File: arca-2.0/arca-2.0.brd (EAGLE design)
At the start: 355.6 x 127 mm, 192 parts, among them IC1 MCP6N11R, IC2 MCP6N11R, IC3 MCP6N11R, IC4 MCP6N11R, IC5 LM324D, IC6 LM324D, SW1 1101M2S3CQE2, SW2 1101M2S3CQE2, T1 FQP30N06L, T2 FQP30N06L, T3 FQP30N06L, T4 FQP30N06L, T5 FQP30N06L, T6 FQP30N06L, X1 2540-5

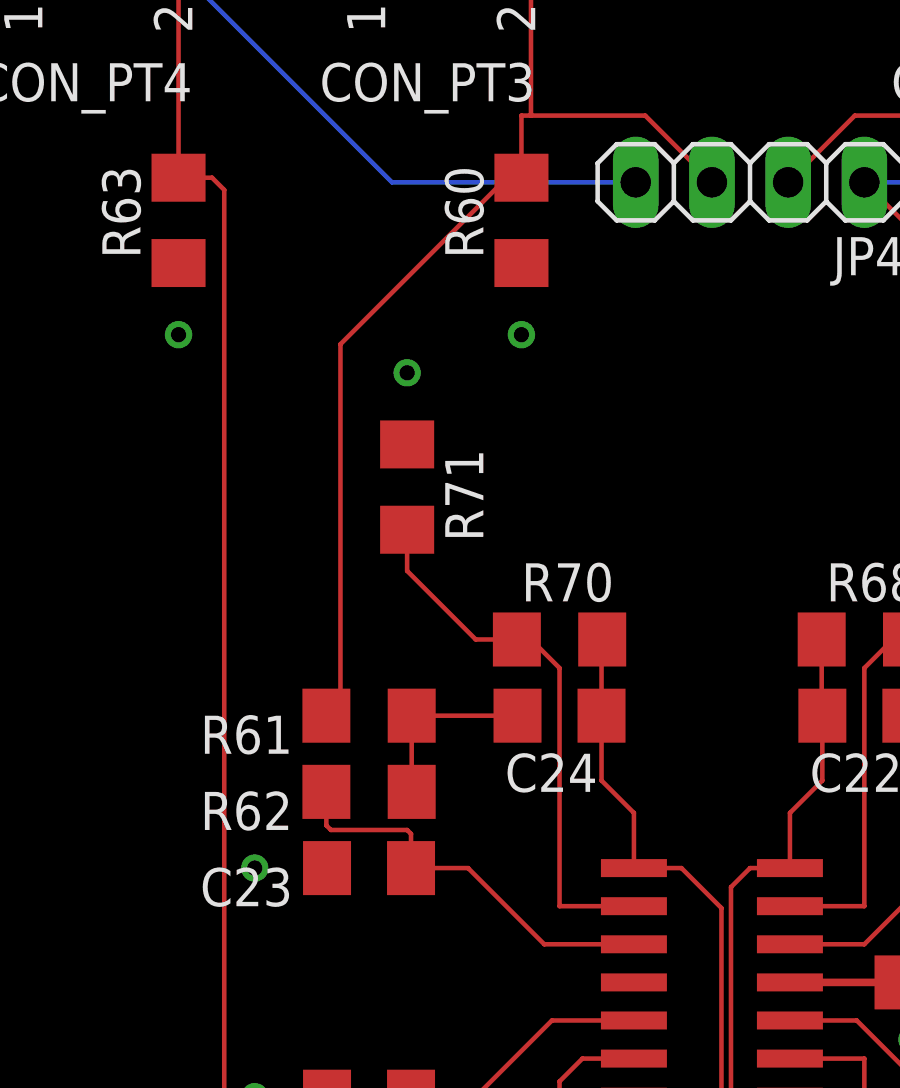
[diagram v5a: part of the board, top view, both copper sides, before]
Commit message: resistor cleanup for v_ref
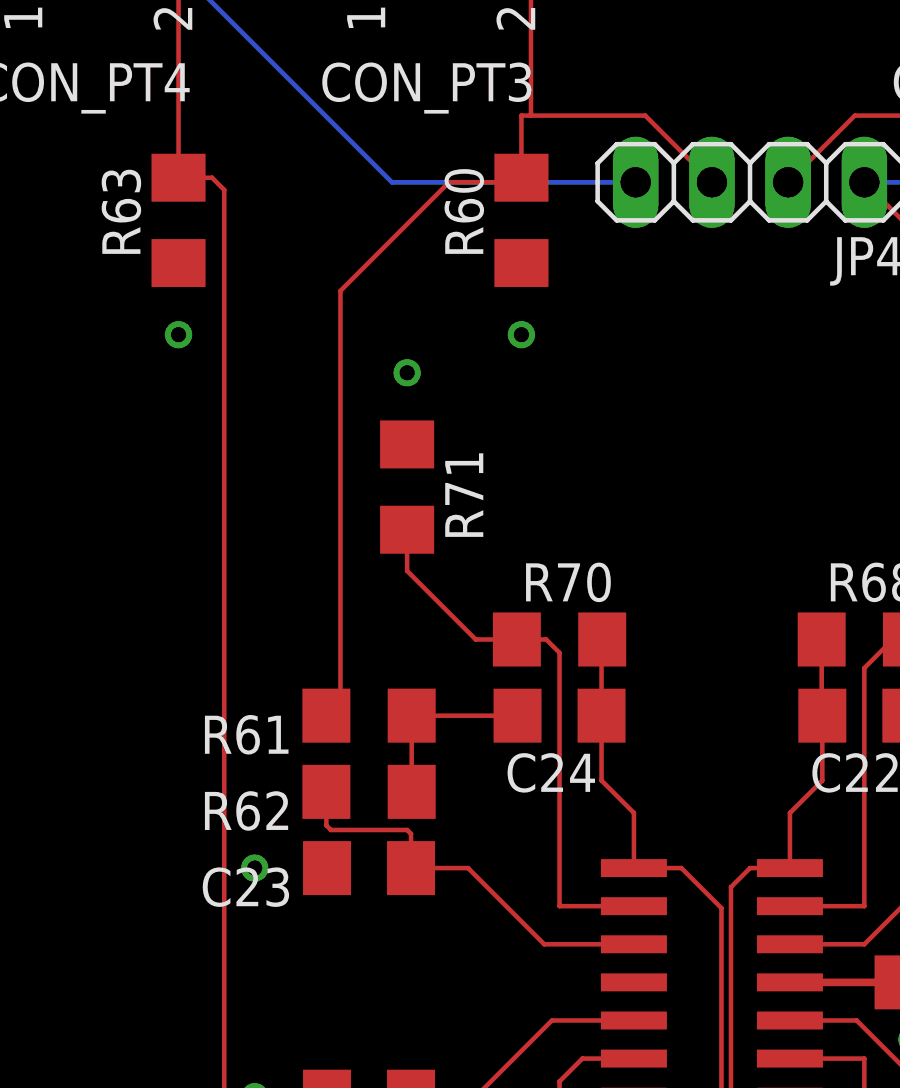
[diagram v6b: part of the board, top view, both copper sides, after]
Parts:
- R46, R48, R50, R52: value 10k -> 43k
- R47, R49, R51, R53: value 10k -> 11k
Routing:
- net PT3-: track 46.7 -> 47.7 mm
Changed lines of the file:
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@@
 <?xml version="1.0" encoding="utf-8"?>
 <!DOCTYPE eagle SYSTEM "eagle.dtd">
-<eagle version="9.5.0">
+<eagle version="9.6.2">
 <drawing>
 <settings>
@@
 <attribute name="VALUE" x="311.15" y="12.7" size="1.27" layer="27" rot="R270"/>
 </element>
-<element name="R46" library="rcl" library_urn="urn:adsk.eagle:library:334" package="R1206" package3d_urn="urn:adsk.eagle:package:23540/2" value="10k" x="139.7" y="81.28" smashed="yes">
+<element name="R46" library="rcl" library_urn="urn:adsk.eagle:library:334" package="R1206" package3d_urn="urn:adsk.eagle:package:23540/2" value="43k" x="139.7" y="81.28" smashed="yes">
 <attribute name="NAME" x="138.43" y="82.55" size="1.27" layer="25"/>
 <attribute name="POPULARITY" value="19" x="139.7" y="81.28" size="1.778" layer="27" display="off"/>
@@
 <attribute name="VALUE" x="138.43" y="78.74" size="1.27" layer="27"/>
 </element>
-<element name="R47" library="rcl" library_urn="urn:adsk.eagle:library:334" package="R1206" package3d_urn="urn:adsk.eagle:package:23540/2" value="10k" x="139.7" y="78.74" smashed="yes" rot="R180">
+<element name="R47" library="rcl" library_urn="urn:adsk.eagle:library:334" package="R1206" package3d_urn="urn:adsk.eagle:package:23540/2" value="11k" x="139.7" y="78.74" smashed="yes" rot="R180">
 <attribute name="NAME" x="140.97" y="77.47" size="1.27" layer="25" rot="R180"/>
 <attribute name="POPULARITY" value="19" x="139.7" y="78.74" size="1.778" layer="27" rot="R180" display="off"/>
@@
 <attribute name="VALUE" x="140.97" y="81.28" size="1.27" layer="27" rot="R180"/>
 </element>
-<element name="R48" library="rcl" library_urn="urn:adsk.eagle:library:334" package="R1206" package3d_urn="urn:adsk.eagle:package:23540/2" value="10k" x="118.11" y="81.28" smashed="yes">
+<element name="R48" library="rcl" library_urn="urn:adsk.eagle:library:334" package="R1206" package3d_urn="urn:adsk.eagle:package:23540/2" value="43k" x="118.11" y="81.28" smashed="yes">
 <attribute name="NAME" x="116.84" y="82.55" size="1.27" layer="25"/>
 <attribute name="POPULARITY" value="19" x="118.11" y="81.28" size="1.778" layer="27" display="off"/>
@@
 <attribute name="VALUE" x="116.84" y="78.74" size="1.27" layer="27"/>
 </element>
-<element name="R49" library="rcl" library_urn="urn:adsk.eagle:library:334" package="R1206" package3d_urn="urn:adsk.eagle:package:23540/2" value="10k" x="118.11" y="78.74" smashed="yes" rot="R180">
+<element name="R49" library="rcl" library_urn="urn:adsk.eagle:library:334" package="R1206" package3d_urn="urn:adsk.eagle:package:23540/2" value="11k" x="118.11" y="78.74" smashed="yes" rot="R180">
 <attribute name="NAME" x="119.38" y="77.47" size="1.27" layer="25" rot="R180"/>
 <attribute name="POPULARITY" value="19" x="118.11" y="78.74" size="1.778" layer="27" rot="R180" display="off"/>
@@
 <attribute name="VALUE" x="119.38" y="81.28" size="1.27" layer="27" rot="R180"/>
 </element>
-<element name="R50" library="rcl" library_urn="urn:adsk.eagle:library:334" package="R1206" package3d_urn="urn:adsk.eagle:package:23540/2" value="10k" x="96.52" y="81.28" smashed="yes">
+<element name="R50" library="rcl" library_urn="urn:adsk.eagle:library:334" package="R1206" package3d_urn="urn:adsk.eagle:package:23540/2" value="43k" x="96.52" y="81.28" smashed="yes">
 <attribute name="NAME" x="95.25" y="82.55" size="1.27" layer="25"/>
 <attribute name="POPULARITY" value="19" x="96.52" y="81.28" size="1.778" layer="27" display="off"/>
@@
 <attribute name="VALUE" x="95.25" y="78.74" size="1.27" layer="27"/>
 </element>
-<element name="R51" library="rcl" library_urn="urn:adsk.eagle:library:334" package="R1206" package3d_urn="urn:adsk.eagle:package:23540/2" value="10k" x="96.52" y="78.74" smashed="yes" rot="R180">
+<element name="R51" library="rcl" library_urn="urn:adsk.eagle:library:334" package="R1206" package3d_urn="urn:adsk.eagle:package:23540/2" value="11k" x="96.52" y="78.74" smashed="yes" rot="R180">
 <attribute name="NAME" x="97.79" y="77.47" size="1.27" layer="25" rot="R180"/>
 <attribute name="POPULARITY" value="19" x="96.52" y="78.74" size="1.778" layer="27" rot="R180" display="off"/>
@@
 <attribute name="VALUE" x="97.79" y="81.28" size="1.27" layer="27" rot="R180"/>
 </element>
-<element name="R52" library="rcl" library_urn="urn:adsk.eagle:library:334" package="R1206" package3d_urn="urn:adsk.eagle:package:23540/2" value="10k" x="74.93" y="81.28" smashed="yes">
+<element name="R52" library="rcl" library_urn="urn:adsk.eagle:library:334" package="R1206" package3d_urn="urn:adsk.eagle:package:23540/2" value="43k" x="74.93" y="81.28" smashed="yes">
 <attribute name="NAME" x="73.66" y="82.55" size="1.27" layer="25"/>
 <attribute name="POPULARITY" value="19" x="74.93" y="81.28" size="1.778" layer="27" display="off"/>
@@
 <attribute name="VALUE" x="73.66" y="78.74" size="1.27" layer="27"/>
 </element>
-<element name="R53" library="rcl" library_urn="urn:adsk.eagle:library:334" package="R1206" package3d_urn="urn:adsk.eagle:package:23540/2" value="10k" x="74.93" y="78.74" smashed="yes" rot="R180">
+<element name="R53" library="rcl" library_urn="urn:adsk.eagle:library:334" package="R1206" package3d_urn="urn:adsk.eagle:package:23540/2" value="11k" x="74.93" y="78.74" smashed="yes" rot="R180">
 <attribute name="NAME" x="76.2" y="77.47" size="1.27" layer="25" rot="R180"/>
 <attribute name="POPULARITY" value="19" x="74.93" y="78.74" size="1.778" layer="27" rot="R180" display="off"/>
@@
 <contactref element="JP4" pad="3"/>
 <wire x1="25.7175" y1="80.3275" x2="25.4" y2="80.01" width="0.1524" layer="1"/>
-<wire x1="25.7175" y1="92.3925" x2="25.7175" y2="80.3275" width="0.1524" layer="1"/>
-<wire x1="31.115" y1="97.79" x2="25.7175" y2="92.3925" width="0.1524" layer="1"/>
-<wire x1="31.75" y1="97.79" x2="31.115" y2="97.79" width="0.1524" layer="1"/>
+<wire x1="25.7175" y1="94.1705" x2="25.7175" y2="80.3275" width="0.1524" layer="1"/>
+<wire x1="29.337" y1="97.79" x2="25.7175" y2="94.1705" width="0.1524" layer="1"/>
+<wire x1="31.75" y1="97.79" x2="29.337" y2="97.79" width="0.1524" layer="1"/>
 <wire x1="25.4" y1="80.01" x2="25.248" y2="80.01" width="0.1524" layer="1"/>
 <wire x1="31.75" y1="97.79" x2="31.75" y2="97.942" width="0.1524" layer="1"/>
@@
 <wire x1="31.598" y1="82.55" x2="30.226" y2="82.55" width="0.1524" layer="1"/>
 <wire x1="33.02" y1="73.66" x2="35.5" y2="73.66" width="0.1524" layer="1"/>
-<wire x1="33.02" y1="81.5975" x2="33.02" y2="73.66" width="0.1524" layer="1"/>
-<wire x1="32.0675" y1="82.55" x2="33.02" y2="81.5975" width="0.1524" layer="1"/>
-<wire x1="31.598" y1="82.55" x2="32.0675" y2="82.55" width="0.1524" layer="1"/>
+<wire x1="33.02" y1="82.1055" x2="33.02" y2="73.66" width="0.1524" layer="1"/>
+<wire x1="32.5755" y1="82.55" x2="33.02" y2="82.1055" width="0.1524" layer="1"/>
+<wire x1="31.598" y1="82.55" x2="32.5755" y2="82.55" width="0.1524" layer="1"/>
 </signal>
 <signal name="N$46">

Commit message: separate fuses for each external connection + LM324s on +10V
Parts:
- added FS10, FS11, FS12, FS13, FS14, FS15, FS16, FS17, FS18, FS9: 178.6165, fuse-holder-littlefuse:178.6165
- moved FS8 293.2 mm to (-35.6, -53.1), turned to 0 degrees
- moved FS7 156.3 mm to (-35.6, -41.7), turned to 0 degrees
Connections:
- removed net +10V_FS: CON_PT1.1, CON_PT1.2, CON_PT2.1, CON_PT2.2, CON_PT3.1, CON_PT3.2, CON_PT4.1, CON_PT4.2, FS7.1, FS7.2, FS7.3, FS7.4
- removed net +5V_FS: CON_LC1.1, CON_LC1.2, CON_LC2.1, CON_LC2.2, CON_LC3.1, CON_LC3.2, CON_LC4.1, CON_LC4.2, CON_TC1.1, CON_TC1.2, CON_TC2.1, CON_TC2.2, CON_TC3.1, CON_TC3.2, CON_TC4.1, CON_TC4.2, FS8.1, FS8.2, FS8.3, FS8.4
- new net N$61: CON_LC1.1, CON_LC1.2, FS7.1, FS7.2, FS7.3, FS7.4
- new net N$62: CON_LC2.1, CON_LC2.2, FS8.1, FS8.2, FS8.3, FS8.4
- new net N$63: CON_LC3.1, CON_LC3.2, FS9.1, FS9.2, FS9.3, FS9.4
- new net N$64: CON_LC4.1, CON_LC4.2, FS10.1, FS10.2, FS10.3, FS10.4
- new net N$65: CON_PT1.1, CON_PT1.2, FS11.1, FS11.2, FS11.3, FS11.4
- new net N$66: CON_PT2.1, CON_PT2.2, FS12.1, FS12.2, FS12.3, FS12.4
- new net N$69: CON_PT3.1, CON_PT3.2, FS13.1, FS13.2, FS13.3, FS13.4
- new net N$70: CON_PT4.1, CON_PT4.2, FS14.1, FS14.2, FS14.3, FS14.4
- new net N$71: CON_TC1.1, CON_TC1.2, FS15.1, FS15.2, FS15.3, FS15.4
- new net N$72: CON_TC2.1, CON_TC2.2, FS16.1, FS16.2, FS16.3, FS16.4
- new net N$73: CON_TC3.1, CON_TC3.2, FS17.1, FS17.2, FS17.3, FS17.4
- new net N$74: CON_TC4.1, CON_TC4.2, FS18.1, FS18.2, FS18.3, FS18.4
- net +10V: now also C11.1, C20.1, FS11.5, FS11.6, FS11.7, FS11.8, FS12.5, FS12.6, FS12.7, FS12.8, FS13.5, FS13.6, FS13.7, FS13.8, FS14.5, FS14.6, FS14.7, FS14.8, IC5.4, IC6.4; no longer FS7.5, FS7.6, FS7.7, FS7.8
- net +5V: now also FS10.5, FS10.6, FS10.7, FS10.8, FS15.5, FS15.6, FS15.7, FS15.8, FS16.5, FS16.6, FS16.7, FS16.8, FS17.5, FS17.6, FS17.7, FS17.8, FS18.5, FS18.6, FS18.7, FS18.8, FS7.5, FS7.6, FS7.7, FS7.8, FS9.5, FS9.6, FS9.7, FS9.8; no longer C11.1, C20.1, IC5.4, IC6.4
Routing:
- net +5V_FS: track 256.5 -> 0.00 mm
- net +10V_FS: track 112.7 -> 0.00 mm
- net +5V: track 685.0 -> 669.1 mm
- net +10V: track 166.8 -> 163.1 mm

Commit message: laying out extra breakers in board
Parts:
- moved FS15 331.8 mm to (211.1, 88.9), turned to 270 degrees
- moved FS16 324.2 mm to (189.5, 88.9), turned to 270 degrees
- moved FS17 318.4 mm to (167.9, 88.9), turned to 270 degrees
- moved FS18 314.3 mm to (146.3, 88.9), turned to 270 degrees
- moved FS14 216.4 mm to (14.2, 88.9), turned to 270 degrees
- moved FS13 208.3 mm to (25.7, 88.9), turned to 270 degrees
- moved FS7 206.7 mm to (124.7, 88.9), turned to 270 degrees
- moved FS12 201.3 mm to (37.1, 88.9), turned to 270 degrees
- moved FS8 198.5 mm to (103.1, 88.9), turned to 270 degrees
- moved FS11 195.3 mm to (48.5, 88.9), turned to 270 degrees
- moved FS9 193.0 mm to (81.5, 88.9), turned to 270 degrees
- moved FS10 190.5 mm to (59.9, 88.9), turned to 270 degrees
- moved ADC3 147.5 mm to (182.9, 68.6)
- moved ADC1 140.6 mm to (63.5, 27.9)
- moved ADC2 56.8 mm to (31.8, 17.8), turned to 180 degrees
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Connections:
- net ADC1_CS: now also R74.1, X1.22; no longer R76.1, X1.26
- net ADC2_CS: now also R75.1; no longer R74.1
- net ADC3_CS: now also R76.1, X1.26; no longer R75.1, X1.22
- net LC1_CAL: now also ADC1.1; no longer ADC2.1
- net LC2_CAL: now also ADC1.2; no longer ADC2.2
- net LC3_CAL: now also ADC1.3; no longer ADC2.3
- net LC4_CAL: now also ADC1.4; no longer ADC2.4
- net N$49: now also ADC3.5; no longer ADC1.5
- net N$50: now also ADC3.6; no longer ADC1.6
- net N$51: now also ADC3.7; no longer ADC1.7
- net N$52: now also ADC3.8; no longer ADC1.8
- net N$53: now also ADC1.8; no longer ADC2.8
- net N$54: now also ADC1.7; no longer ADC2.7
- net N$55: now also ADC1.6; no longer ADC2.6
- net N$56: now also ADC1.5; no longer ADC2.5
- net N$57: now also ADC2.5; no longer ADC3.5
- net N$58: now also ADC2.6; no longer ADC3.6
- net N$59: now also ADC2.7; no longer ADC3.7
- net N$60: now also ADC2.8; no longer ADC3.8
- net PT1_CAL: now also ADC2.1; no longer ADC3.1
- net PT2_CAL: now also ADC2.2; no longer ADC3.2
- net PT3_CAL: now also ADC2.3; no longer ADC3.3
- net PT4_CAL: now also ADC2.4; no longer ADC3.4
- net TC1: now also ADC3.1; no longer ADC1.1
- net TC2: now also ADC3.2; no longer ADC1.2
- net TC3: now also ADC3.3; no longer ADC1.3
- net TC4: now also ADC3.4; no longer ADC1.4
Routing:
- net +10V: track 163.1 -> 291.1 mm, vias 1 -> 2
- net ADC1_CS: track 124.5 -> 33.8 mm, vias 0 -> 1
- net +5V: track 669.1 -> 744.8 mm, vias 15 -> 4
- net ADC3_CS: track 73.6 -> 127.2 mm, vias 0 -> 1
- net +12V: track 329.3 -> 281.5 mm, vias 1 -> 2
- net LC2+: track 28.8 -> 61.7 mm
- net N$63: track 0.00 -> 31.6 mm
- net N$71: track 0.00 -> 31.6 mm
- net N$69: track 0.00 -> 31.6 mm
- net N$66: track 0.00 -> 31.5 mm
- net N$65: track 0.00 -> 31.5 mm
- net N$70: track 0.00 -> 31.5 mm
- net N$61: track 0.00 -> 31.3 mm
- net N$73: track 0.00 -> 31.3 mm
- net N$72: track 0.00 -> 31.3 mm
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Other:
- board size 355.6 x 127 mm -> 336.6 x 127 mm
